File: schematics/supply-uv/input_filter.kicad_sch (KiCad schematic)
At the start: 42 parts, among them J5 CW2B-10A-T, K1 SRD-12VDC-SL-C, U1 ICE2PCS01, U2 TL331, Y3 B32022A3223M000

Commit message: Boards prepared to order
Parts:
- R1, R3, R4: footprint Resistor_THT:R_Axial_DIN0411_L9.9mm_D3.6mm_P7.62mm_Vertical -> Resistor_THT:R_Axial_DIN0516_L15.5mm_D5.0mm_P7.62mm_Vertical
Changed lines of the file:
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@@
       (effects (font (size 1.27 1.27)))
     )
-    (property "Footprint" "Resistor_THT:R_Axial_DIN0411_L9.9mm_D3.6mm_P7.62mm_Vertical" (at 208.28 56.388 90)
+    (property "Footprint" "Resistor_THT:R_Axial_DIN0516_L15.5mm_D5.0mm_P7.62mm_Vertical" (at 208.28 56.388 90)
       (effects (font (size 1.27 1.27)) hide)
     )
@@
       (effects (font (size 1.27 1.27)))
     )
-    (property "Footprint" "Resistor_THT:R_Axial_DIN0411_L9.9mm_D3.6mm_P7.62mm_Vertical" (at 219.71 56.388 90)
+    (property "Footprint" "Resistor_THT:R_Axial_DIN0516_L15.5mm_D5.0mm_P7.62mm_Vertical" (at 219.71 56.388 90)
       (effects (font (size 1.27 1.27)) hide)
     )
@@
       (effects (font (size 1.27 1.27)))
     )
-    (property "Footprint" "Resistor_THT:R_Axial_DIN0411_L9.9mm_D3.6mm_P7.62mm_Vertical" (at 231.14 56.388 90)
-      (effects (font (size 1.27 1.27)) hide)
-    )
+    (property "Footprint" "Resistor_THT:R_Axial_DIN0516_L15.5mm_D5.0mm_P7.62mm_Vertical" (at 231.14 56.388 90)
+      (effects (font (size 1.27 1.27)) hide)
+    )

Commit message: Found and fixed issues in schematics.
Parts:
- removed TP2: 400V, TestPoint:TestPoint_Pad_2.0x2.0mm, symbol Connector:TestPoint
- added CLR2: HS077@20x15x10mm, Library:HS-077, symbol My_Library:COOLER
- added RP2: 0.12, Resistor_SMD:R_2512_6332Metric, symbol Device:R
- R1, R3, R4: footprint Resistor_THT:R_Axial_DIN0516_L15.5mm_D5.0mm_P7.62mm_Vertical -> Varistor:RV_Disc_D12mm_W5.8mm_P7.5mm
- RP1: value 20K -> 33K
- RP10, RP9: value 750K -> 680K
- RP11: value 750K -> 620K
- RP12: value 17K -> 15K
- RP16: value 60K -> 62K
- RP2: value 0.01 -> 0.12
- RP8: value 70K -> 75K
- TR1: value ETD 34/17/11@N87@s=5mm N25@1mm*2 -> ETD 34/17/11@N87@s=3.3mm N27@1mm*2
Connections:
- net HV_GND: now also RP2.2
- net VOUT_PRE_GND: now also RP2.1
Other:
- note added: "33K = 136KHz"
- note removed: "20K = 216 KHz"
- moved on the sheet: RP2

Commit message: Continue soldering and setting up hardware
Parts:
- RP16: value 62K -> 68K
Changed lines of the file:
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@@
       (effects (font (size 1.27 1.27)) (justify left))
     )
-    (property "Value" "62K" (at 208.28 152.4 0)
+    (property "Value" "68K" (at 208.28 152.4 0)
       (effects (font (size 1.27 1.27)) (justify left))
     )

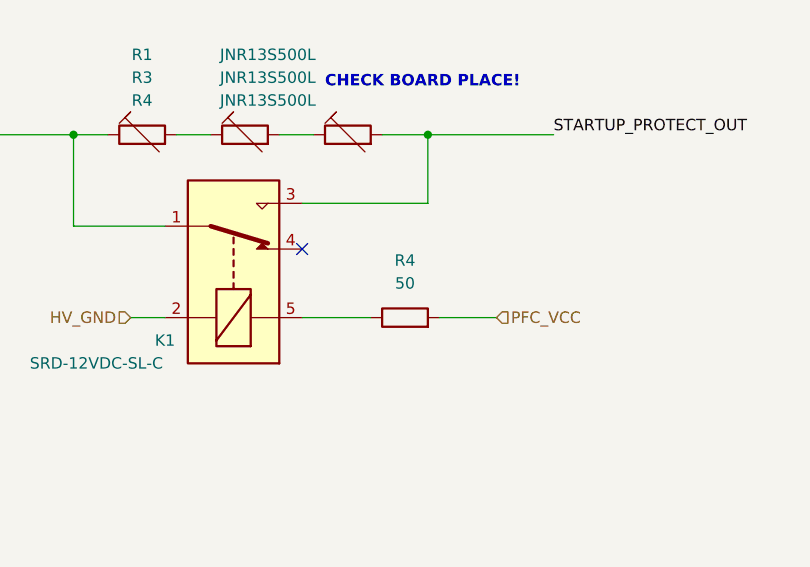
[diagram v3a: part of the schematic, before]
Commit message: some changes in schema. I found additional error. This commit saves changes before re-write some blocks
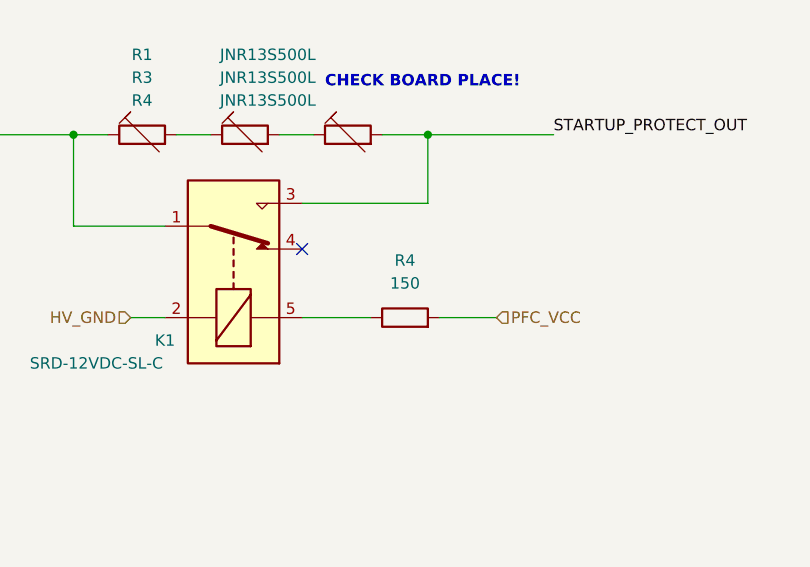
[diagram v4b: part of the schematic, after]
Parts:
- R4: value 50 -> 150

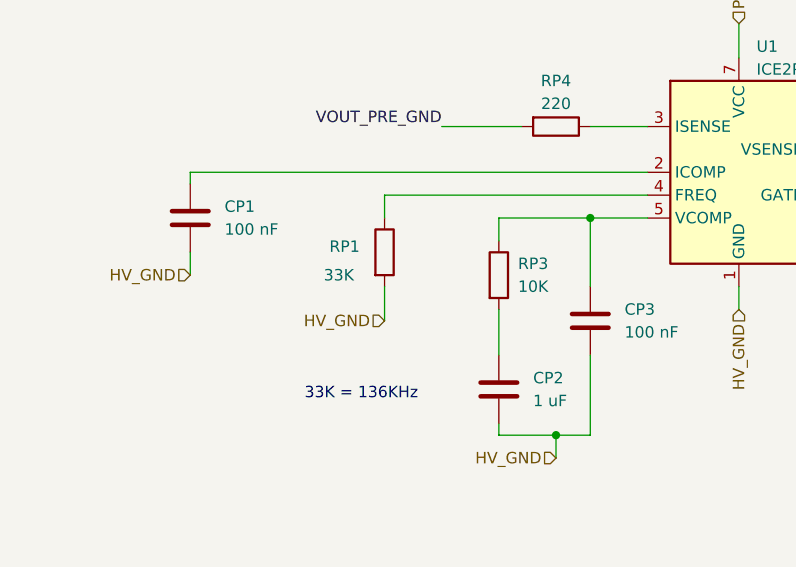
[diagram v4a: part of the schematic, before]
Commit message: debugging DCDC converters... Standby supply works fine (noise level = 1,7%). At now Starting to debug PFC module
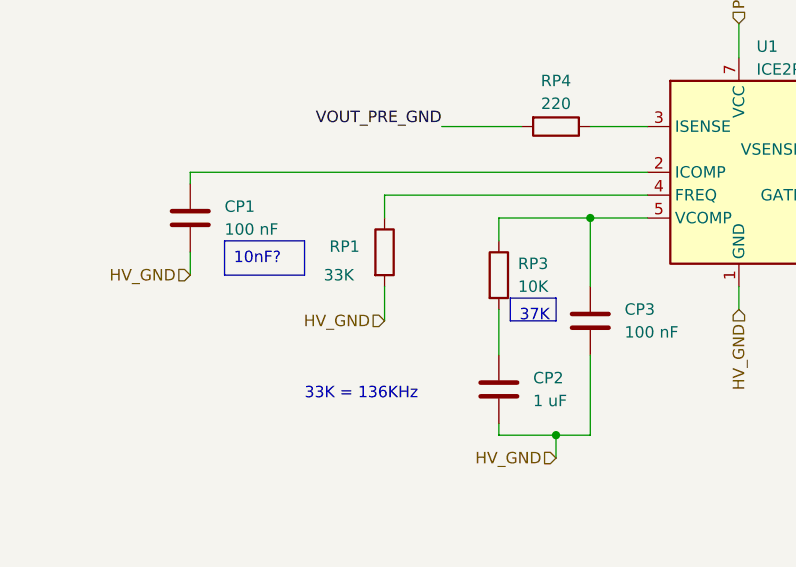
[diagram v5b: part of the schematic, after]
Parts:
- TP1: footprint TestPoint:TestPoint_THTPad_3.0x3.0mm_Drill1.5mm -> Library:TestPoint_Plated_Hole_D1.0mm
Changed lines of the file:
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@@
 		)
 	)
+	(text_box "10nF?"
+		(exclude_from_sim no)
+		(at 36.83 134.62 0)
+		(size 8.89 3.81)
+		(stroke
+			(width 0)
+			(type default)
+		)
+		(fill
+			(type none)
+		)
+		(effects
+			(font
+				(size 1.27 1.27)
+			)
+			(justify left top)
+		)
+	)
+	(text_box "37K"
+		(exclude_from_sim no)
+		(at 68.58 140.97 0)
+		(size 5.08 2.54)
+		(stroke
+			(width 0)
+			(type default)
+		)
+		(fill
+			(type none)
+		)
+		(effects
+			(font
+				(size 1.27 1.27)
+			)
+			(justify left top)
+		)
+	)
 	(text "7A"
 		(exclude_from_sim no)
@@
 			)
 		)
-		(property "Description" ""
+		(property "Description" "Special symbol for telling ERC where power comes from"
 			(at 26.67 19.05 0)
 			(effects
@@
 			)
 		)
-		(property "Footprint" "TestPoint:TestPoint_THTPad_3.0x3.0mm_Drill1.5mm"
+		(property "Footprint" "Library:TestPoint_Plated_Hole_D1.0mm"
 			(at 40.64 21.59 0)
 			(effects
